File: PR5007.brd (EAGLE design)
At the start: 70 x 70 mm, 38 parts

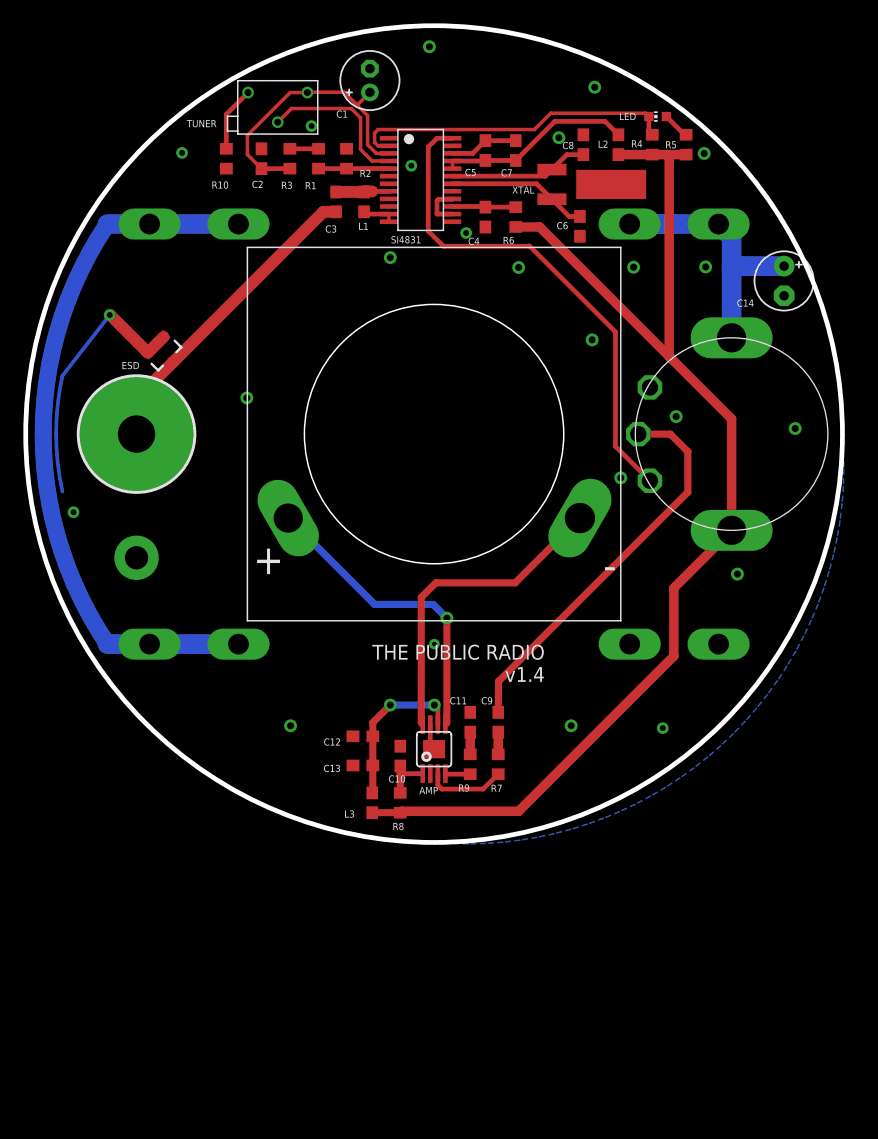
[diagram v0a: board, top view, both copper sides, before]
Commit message: New Board Layout
Made some of the edits based on the workflowy feature request list.
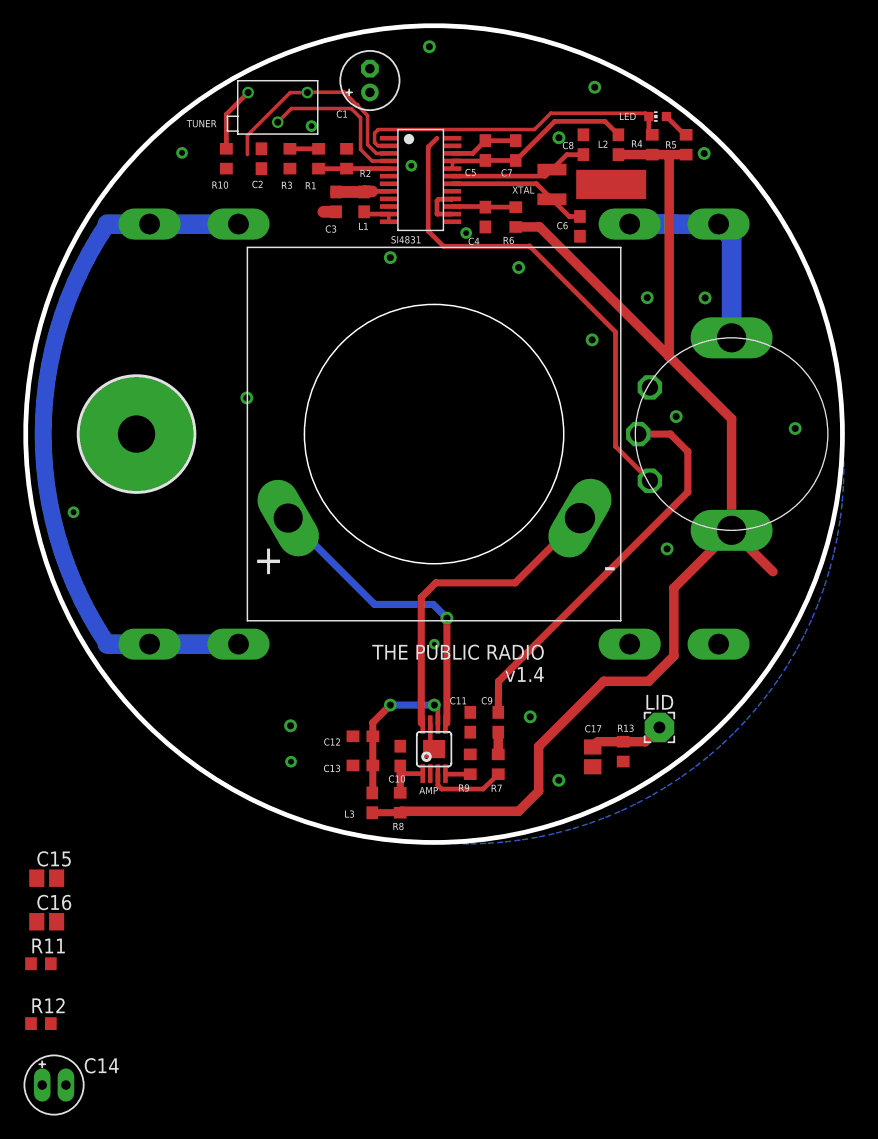
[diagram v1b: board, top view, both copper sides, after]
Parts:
- removed ESD: CM1213A-01SO, SparkFun-DiscreteSemi:SOT23-3
- added C15, C16: (no value), resistor:C0805
- added C17: 470pf, resistor:C0805
- added LID: (no value), wirepad:2,54/1,0
- added R11, R12: 1K, resistor:R0603
- added R13: 0Ohm, resistor:R0603
- C11, C9: value 1uf -> .033uf
- C14: value 220uF -> 220uf; device resistor-copy:E2,5-5 -> CPOL-US-LongPads :E2-5
- R7, R9: value 59K -> 33K
- moved C14 93.1 mm to (2.43, -20.8), turned to 0 degrees
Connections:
- new net N$21: C15.2, R11.2
- new net N$30: C16.2, R12.2
- new net N$31: C15.1, SI4831.23
- new net N$33: C16.1, SI4831.24
- new net N$34: C17.1, LID.1, R13.2
- net GND: now also C11.1, C17.2, R13.1; no longer C11.2, ESD.1, ESD.2
- net N$19: no longer ESD.3
- net N$3: now also C11.2; no longer C11.1
- net N$32: no longer C14.+
- net N$5: now also R11.1, R12.1; no longer SI4831.24
- net VCC: now also C14.+
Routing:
- net GND: track 31.9 -> 8.89 mm, vias 25 -> 23
- net N$19: track 26.8 -> 4.13 mm
- net VCC: track 102.2 -> 109.5 mm
- net N$34: track 0.00 -> 6.41 mm
- net N$22: track 24.7 -> 19.0 mm
- net N$32: track 22.8 -> 18.2 mm
- net N$3: track 1.90 -> 0.00 mm
- net N$5: track 43.2 -> 41.9 mm

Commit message: Updated 5007
Update from 5.14. speaker wires no longer crossing
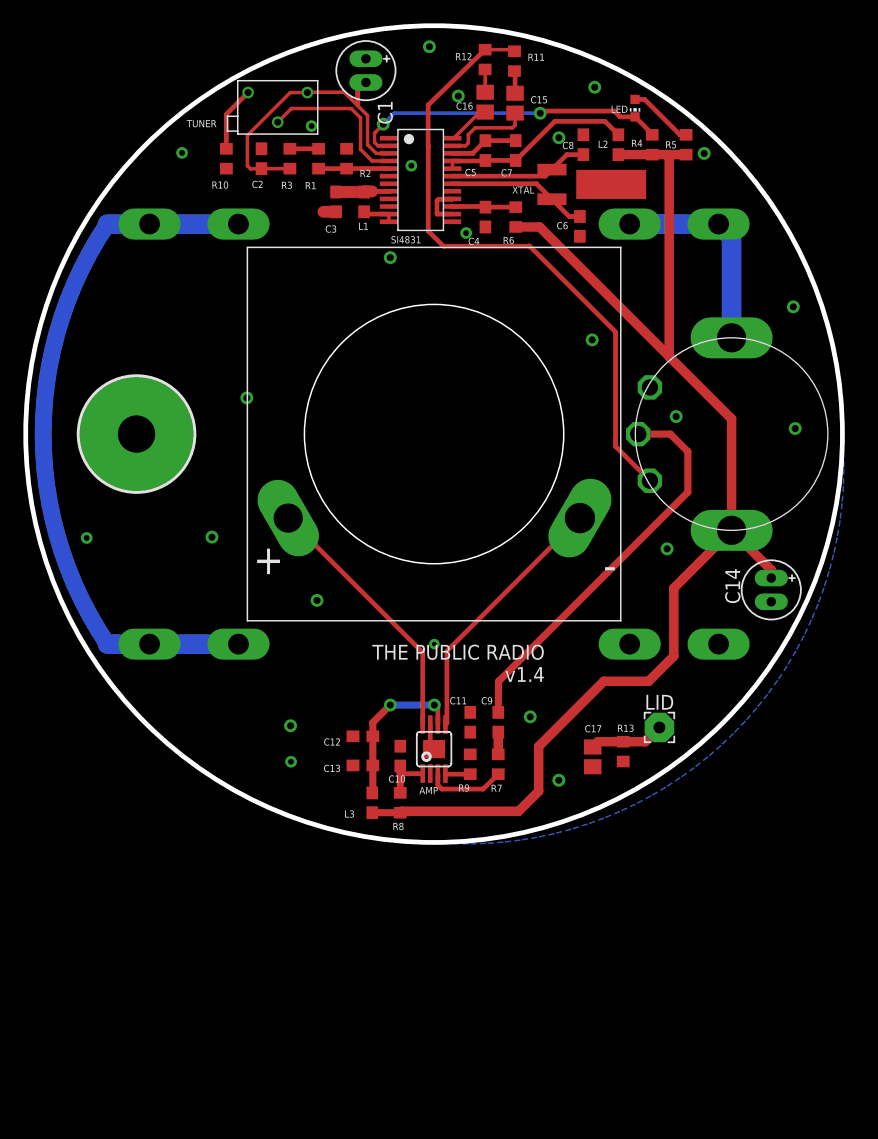
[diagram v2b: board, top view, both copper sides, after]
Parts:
- C1: value 47uF -> 47uf; device resistor-copy:E2-5 -> CPOL-US-LongPads :E2-5
- moved R12 91.0 mm to (39.4, 67.1), turned to 270 degrees
- moved R11 87.4 mm to (41.9, 67.0), turned to 270 degrees
- moved C16 79.7 mm to (39.4, 63.5), turned to 90 degrees
- moved C15 77.6 mm to (41.9, 63.4), turned to 90 degrees
- moved C14 74.7 mm to (63.9, 21.6), turned to 270 degrees
- moved LED 2.06 mm to (52.2, 62.9), turned to 180 degrees
- moved C1 0.92 mm to (29.2, 66.2), turned to 270 degrees
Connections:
- net GND: now also C1.+; no longer C1.-
- net N$22: now also C1.-; no longer C1.+
- net N$23: now also U$3.-; no longer U$3.+
- net N$24: now also U$3.+; no longer U$3.-
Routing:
- net N$5: track 41.9 -> 53.8 mm
- net N$31: track 0.00 -> 7.56 mm
- net N$22: track 19.0 -> 25.9 mm
- net N$24: track 27.4 -> 22.5 mm
- net N$23: track 26.3 -> 22.5 mm, vias 1 -> 0
- net N$33: track 0.00 -> 3.73 mm
- net N$11: track 2.34 -> 5.76 mm
- net N$30: track 0.00 -> 1.95 mm
- net N$21: track 0.00 -> 1.92 mm
- net N$9: track 28.2 -> 28.0 mm, vias 0 -> 2
- net GND: vias 23 -> 24

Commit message: changes from the phone
did pad changes for the trimpot and pot

moved a couple components to start bigger redesign, nothing permanent
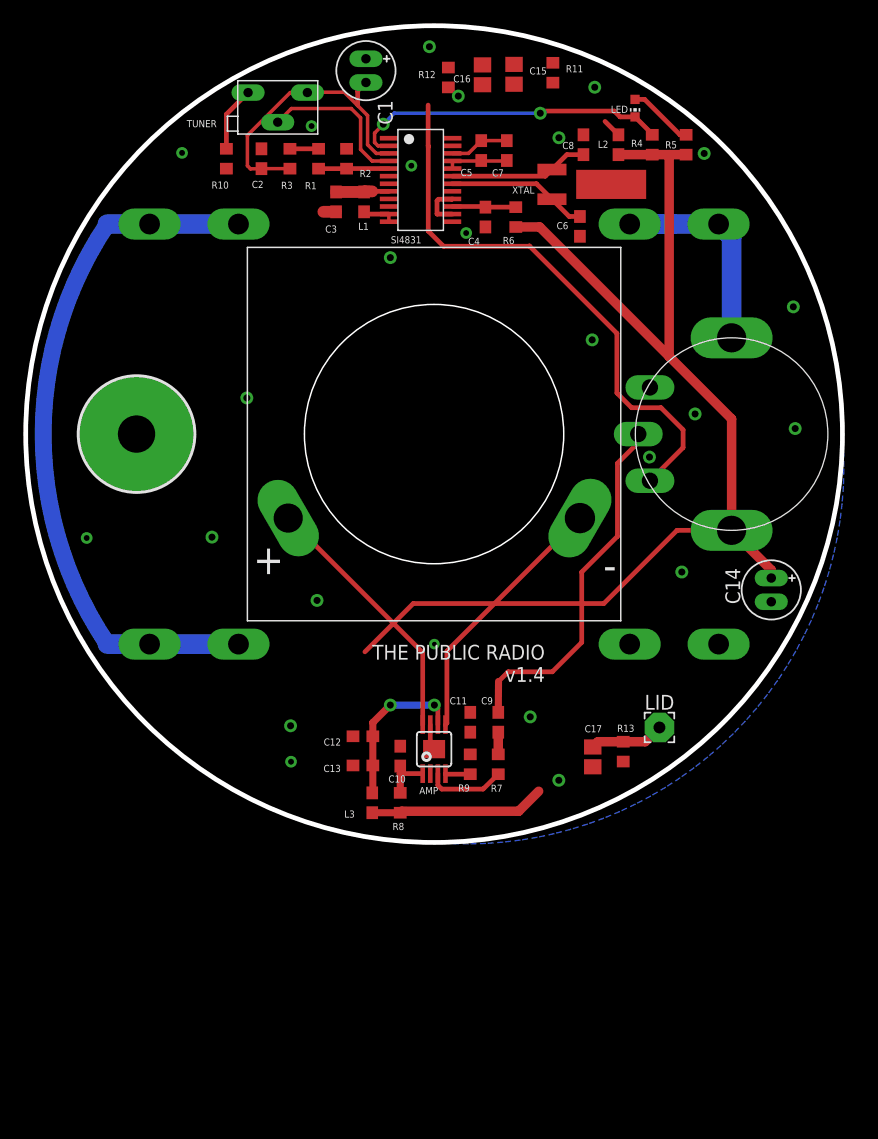
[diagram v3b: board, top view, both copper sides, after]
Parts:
- moved R12 3.50 mm to (36.2, 65.6)
- moved R11 3.43 mm to (45.2, 66.0)
- moved C15 2.48 mm to (41.9, 65.8)
- moved C16 2.35 mm to (39.1, 65.8)
- moved C7 0.77 mm to (41.2, 59.3)
- moved C5 0.36 mm to (39.0, 59.3)
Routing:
- net N$16: track 16.8 -> 6.98 mm
- net N$31: track 7.56 -> 0.00 mm
- net N$5: track 53.8 -> 48.2 mm
- net VCC: track 109.9 -> 114.2 mm
- net N$33: track 3.73 -> 0.11 mm
- net N$25: track 33.9 -> 31.0 mm
- net N$30: track 1.95 -> 0.00 mm
- net N$21: track 1.92 -> 0.00 mm
- net N$6: track 5.88 -> 5.11 mm
- net GND: vias 24 -> 25

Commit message: Updates Post-Phone Call
Added C18,C19,C20 in parallel with existing decoupling caps.
Reworked routing around FM IC and Amp
Added coupling caps and resistors for L+R out.
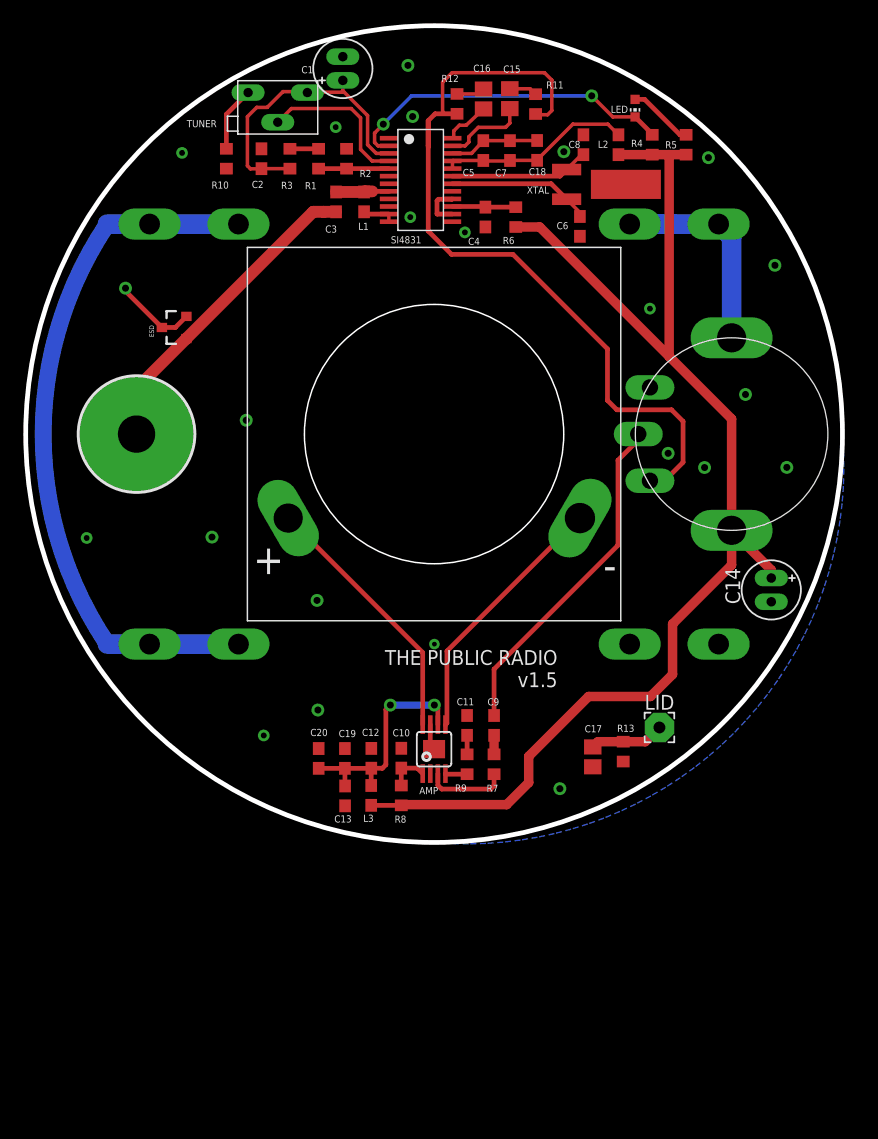
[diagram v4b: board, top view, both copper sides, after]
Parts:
- added C18, C20: 100pf, resistor:C0603
- added C19: 100nf, resistor:C0603
- added ESD: CM1213A-01S, PubRadioLib:SOT23-3
- moved R11 3.07 mm to (43.7, 63.3), turned to 90 degrees
- moved C13 3.03 mm to (27.4, 3.99), turned to 270 degrees
- moved R12 2.38 mm to (37.0, 63.3), turned to 90 degrees
- moved C15 2.12 mm to (41.5, 63.7)
- moved C16 2.07 mm to (39.2, 63.7)
- moved C12 2.02 mm to (29.6, 7.21), turned to 90 degrees
- moved C1 1.99 mm to (27.2, 66.3), turned to 90 degrees
- moved XTAL 1.26 mm to (46.4, 56.4)
- moved L3 0.64 mm to (29.6, 4.03)
- moved R8 0.64 mm to (32.2, 4.03)
- moved C9 0.45 mm to (40.1, 10.0)
- moved C11 0.38 mm to (37.8, 10.0), turned to 270 degrees
- moved R7 0.36 mm to (40.1, 6.70)
- moved C7 0.27 mm to (41.5, 59.3)
- moved R9 0.27 mm to (37.8, 6.70)
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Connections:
- net GND: now also C1.-, C19.2, C20.2, ESD.2, ESD.3; no longer C1.+
- net N$16: now also C18.1
- net N$17: now also C19.1, C20.1
- net N$19: now also ESD.1
- net N$22: now also C1.+; no longer C1.-
- net N$6: now also C18.2
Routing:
- net N$19: track 4.13 -> 27.3 mm
- net N$5: track 48.2 -> 71.3 mm
- net N$16: track 6.98 -> 16.8 mm
- net N$31: track 0.00 -> 7.23 mm
- net GND: track 8.89 -> 16.0 mm, vias 25 -> 23
- net N$17: track 13.7 -> 19.7 mm
- net VCC: track 114.2 -> 109.7 mm
- net N$33: track 0.11 -> 4.05 mm
- net N$6: track 5.11 -> 7.74 mm
- net N$30: track 0.00 -> 2.43 mm
- net N$21: track 0.00 -> 2.40 mm
- net N$25: track 31.0 -> 29.2 mm
- net N$3: track 0.00 -> 1.63 mm
- net N$9: track 28.0 -> 29.1 mm
- net N$18: track 4.22 -> 3.52 mm
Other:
- board text added: "THE PUBLIC RADIO v1.5"
- board text removed: "THE PUBLIC RADIO v1.4"

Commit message: Misc wishlist edits
made LED thru hole.
added restrict on battery clips
moved vcc traces to top layer to avoid bottom ground plane at battery
clips
misc re-routing chages
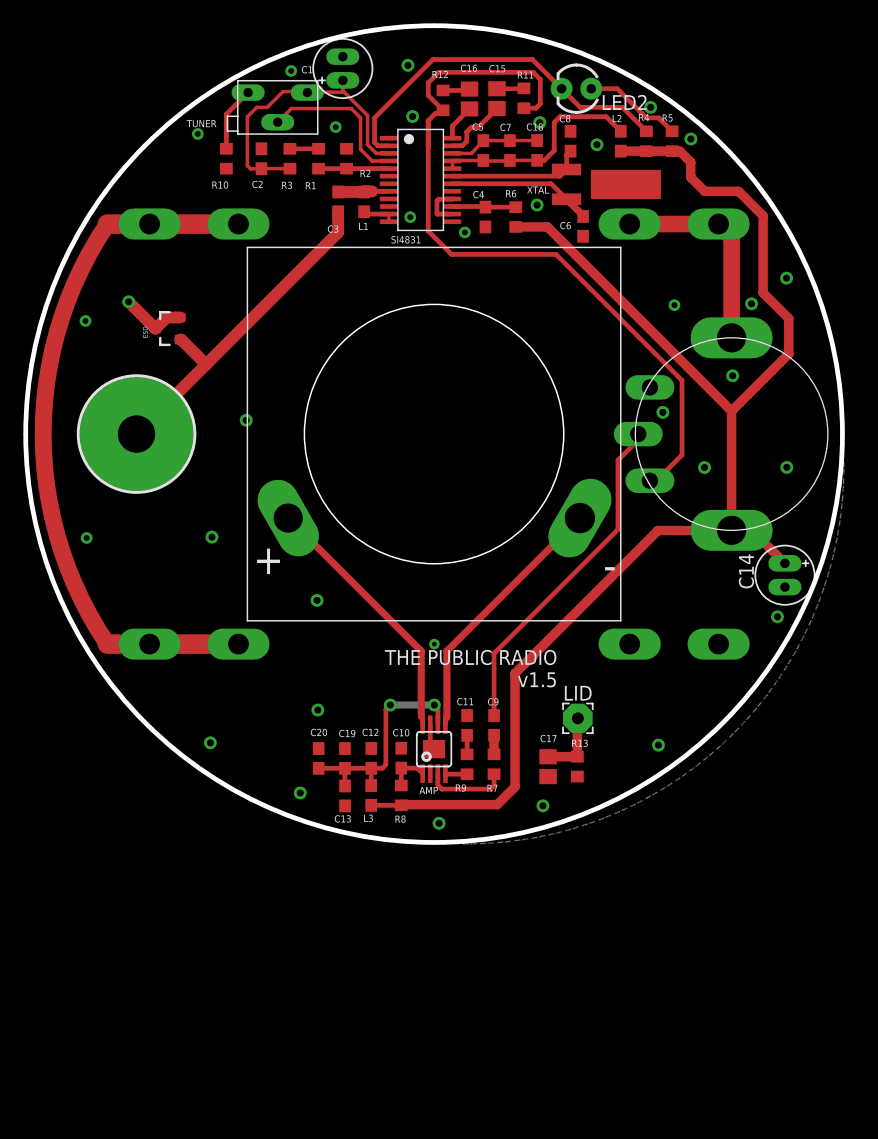
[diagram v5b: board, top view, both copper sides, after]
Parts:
- removed LED: (no value), adafruit:CHIP-LED0603
- added LED2: (no value), SparkFun-LED:LED3MM
- moved LID 7.03 mm to (47.3, 10.6)
- moved R13 4.14 mm to (47.3, 6.50)
- moved C17 3.92 mm to (44.8, 6.50)
- moved C14 1.72 mm to (65.1, 22.9)
- moved R12 1.24 mm to (35.8, 63.6)
- moved R5 1.24 mm to (55.4, 60.1)
- moved C16 1.20 mm to (38.0, 63.7)
- moved C8 1.14 mm to (46.7, 60.1)
- moved R11 1.12 mm to (42.7, 63.8)
- moved C15 1.10 mm to (40.4, 63.7)
- moved R4 0.58 mm to (53.2, 60.1)
- moved ESD 0.55 mm to (12.2, 44.0)
- moved L2 0.36 mm to (51.0, 60.1)
- moved C6 0.27 mm to (47.8, 52.8)
- moved C3 0.18 mm to (26.8, 54.9)
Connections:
- net N$11: now also LED2.A; no longer LED.A
- net N$9: now also LED2.K; no longer LED.C
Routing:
- net VCC: track 109.7 -> 122.5 mm
- net N$5: track 71.3 -> 67.2 mm
- net N$11: track 5.76 -> 8.44 mm
- net N$9: track 29.1 -> 31.4 mm, vias 2 -> 0
- net N$19: track 27.3 -> 29.3 mm
- net N$16: track 16.8 -> 18.8 mm
- net N$31: track 7.23 -> 5.60 mm
- net GND: track 16.0 -> 14.6 mm, vias 23 -> 33
- net N$33: track 4.05 -> 3.12 mm
- net N$34: track 6.41 -> 5.82 mm

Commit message: More Feature Request Updates
Added reverse polarity protection with p-channel mosfet, removed 1K
summing resistors for L&R mix, moved RF IC audio output to the bottom
layer, cleaned up part names and increased size for better print
resolution, added board # and station # markings on the bottom layer.
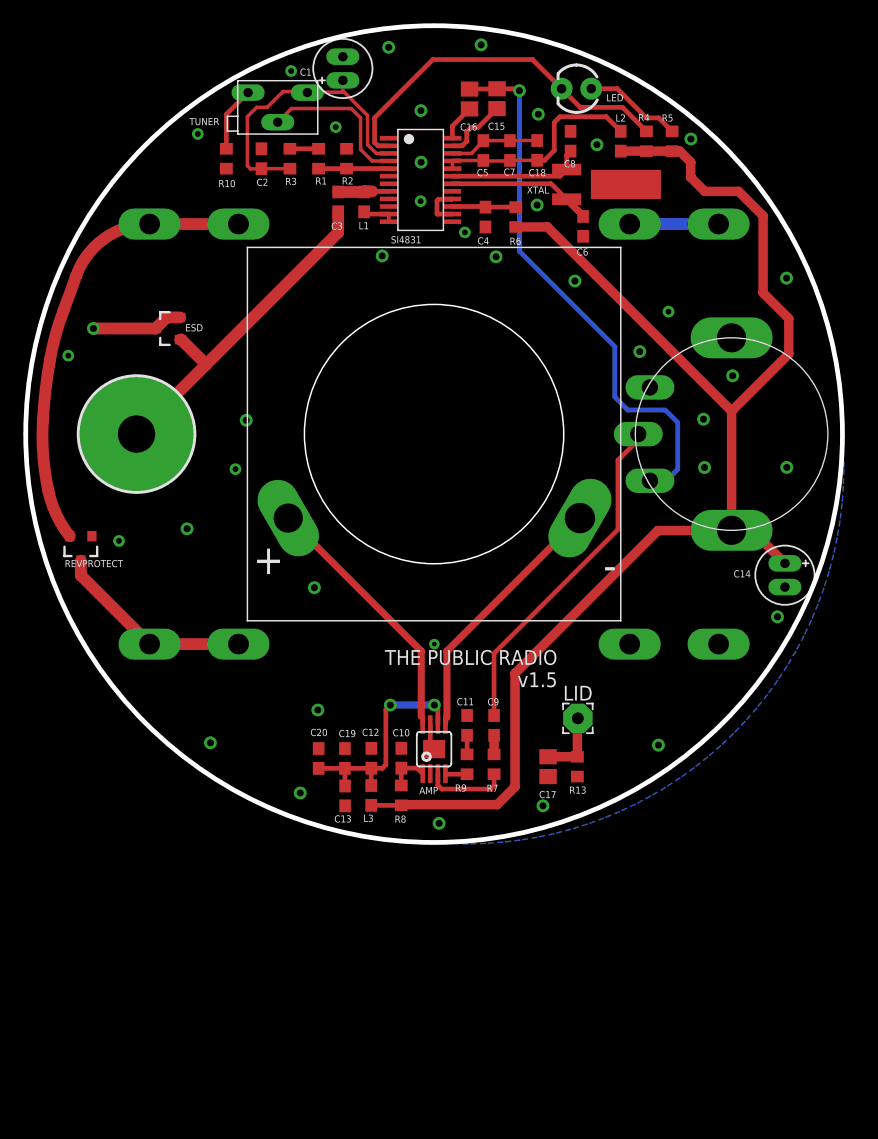
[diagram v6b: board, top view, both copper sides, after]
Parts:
- removed R11, R12: 1K, resistor:R0603
- added REVPROTECT: SI2333DDS, PubRadioLib:SI2333DDS
- renumbered LED2 to LED
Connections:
- removed net N$32: U$1.POS, U$1.POS@2, U$5.SW_OUT
- net GND: now also REVPROTECT.1
- net N$14: now also REVPROTECT.3; no longer U$1.NEG, U$1.NEG@2
- net N$21: now also REVPROTECT.2, U$1.NEG, U$1.NEG@2; no longer C15.2, R11.2
- net N$30: now also U$1.POS, U$1.POS@2; no longer C16.2, R12.2
- net N$5: now also C15.2, C16.2; no longer R11.1, R12.1
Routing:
- net N$14: track 58.5 -> 17.2 mm
- net N$21: track 2.32 -> 38.4 mm
- net N$5: track 67.2 -> 47.1 mm, vias 0 -> 1
- net N$32: track 17.8 -> 0.00 mm
- net N$30: track 2.32 -> 7.62 mm
- net GND: track 14.6 -> 16.7 mm, vias 33 -> 38
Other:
- board text added: "Board"
- board text added: "Board #"
- board text added: "Station"
